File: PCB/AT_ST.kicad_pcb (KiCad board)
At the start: 2 copper layers, 127.3 x 96.8 mm, 84 parts, among them J1 4PIN, J2 OLED, J3 Conn_01x05_Female, J4 Conn_01x05_Female, SW1 SW1, SW10 SW10, SW11 SW11, SW12 SW12, SW13 SW13, SW14 SW14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

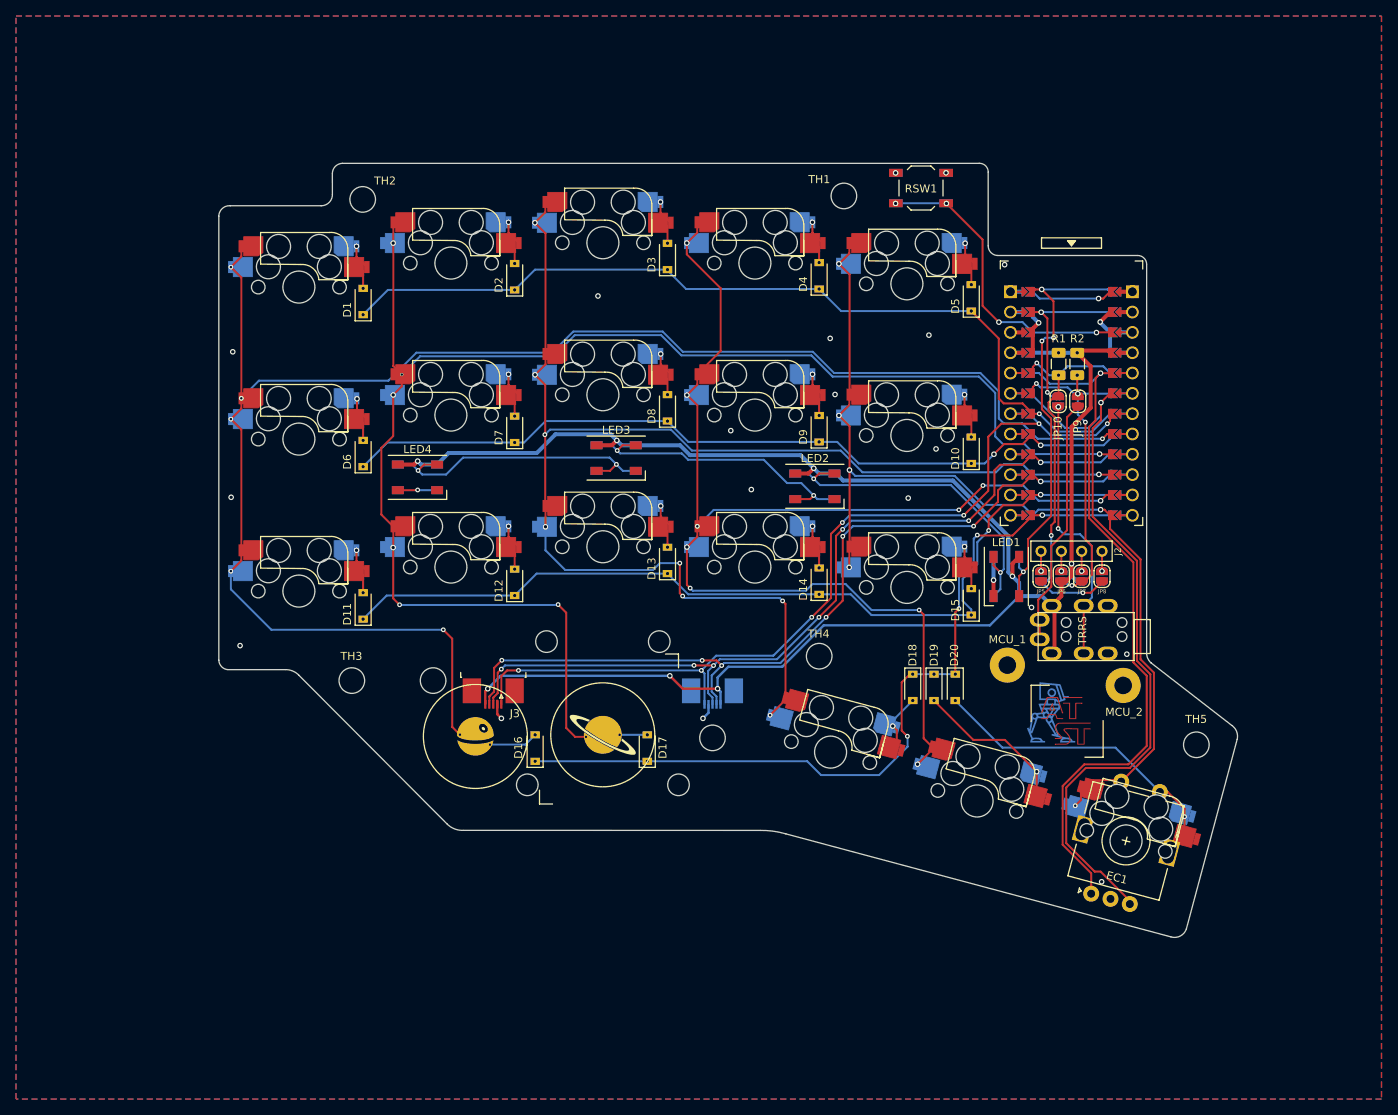
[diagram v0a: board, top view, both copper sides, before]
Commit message: 1. Correct a serious pin allocation problem, where a digital pin was assigned for joystick Y axis. 2. Updated MX switches footprints. 3. Included flip style 5 pins FPC/FFC socket. 4. Minor changes here and there.
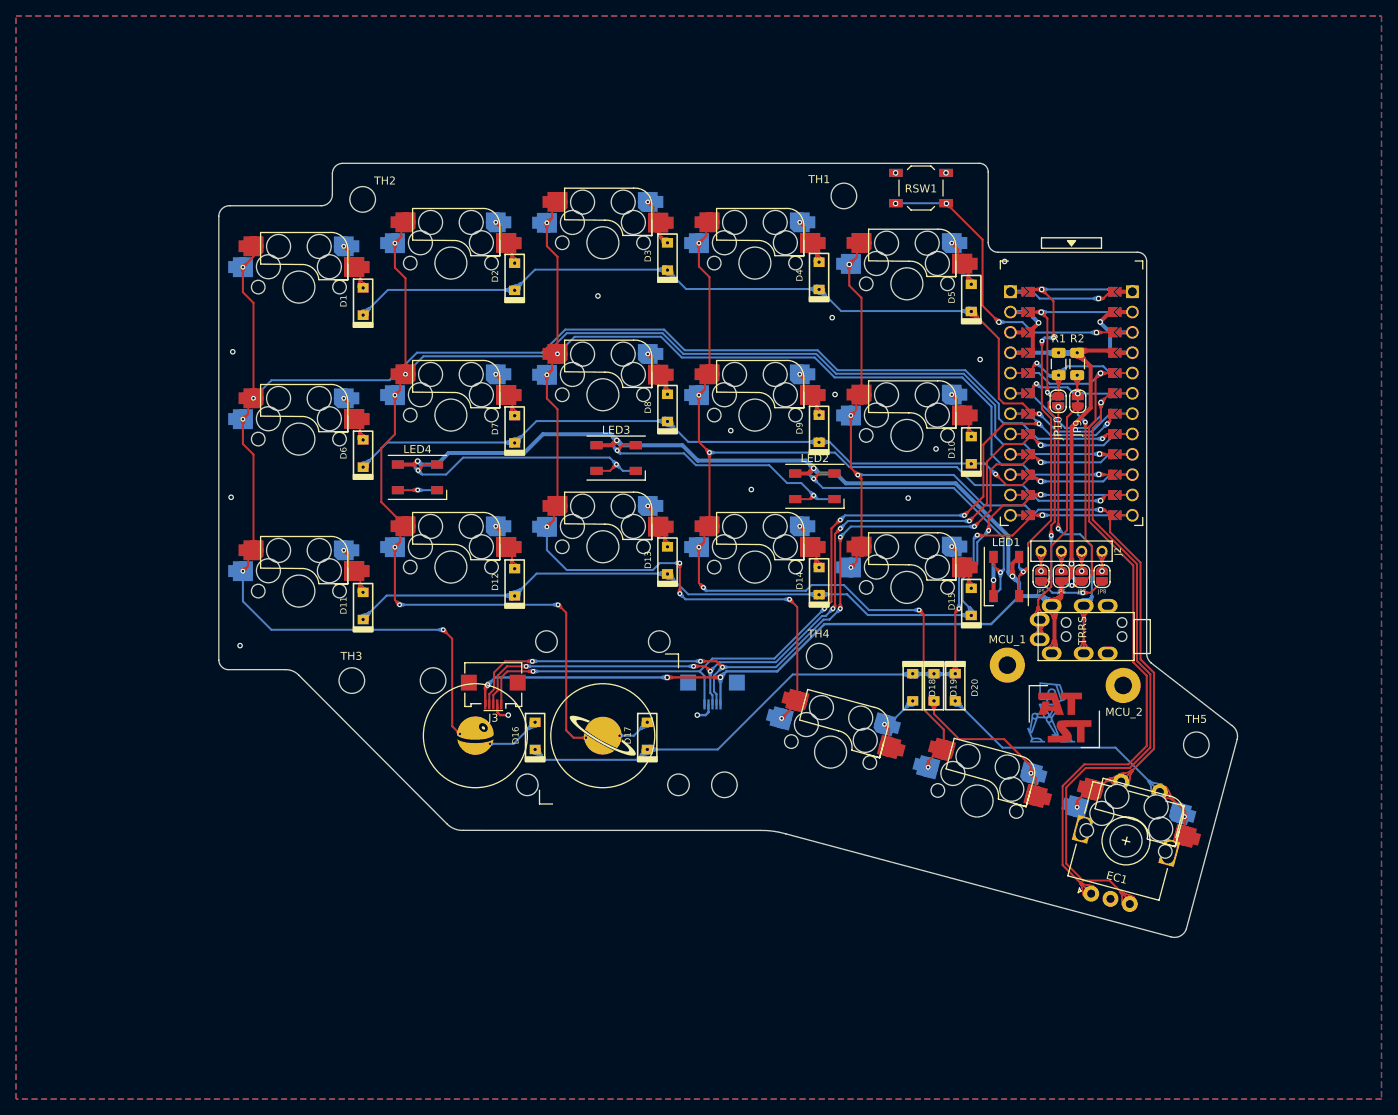
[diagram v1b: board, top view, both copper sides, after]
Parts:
- removed the REF** at (204.0, 128.3)
- added REF**: star_wars_at_st_text_f.cu, jw_custom_image:star_wars_at_st_text_f.cu, F.Cu at (203.8, 127.8)
- D1, D10, D11, D12, D13, D14, D15, D16, D17, D18, D19, D2, D20, D3, D4, D5, D6, D7, D8, D9: footprint jw_custom_footprint:Diode_SOD123_THT -> jw_custom_footprint:Diode_SOD123_THT_2
- J3, J4: footprint Connector_FFC-FPC:TE_0-1734839-5_1x05-1MP_P0.5mm_Horizontal -> jw_custom_footprint:Molex_200528-0050_1x05-1MP_P0.5mm_Horizontal
- moved JY_BT_2 6.05 mm to (161.1, 136.2)
- moved D16 1.52 mm to (137.5, 130.1)
- moved D17 1.52 mm to (151.5, 130.1)
- moved J3 0.44 mm to (132.2, 125.3)
- moved J4 0.44 mm to (159.6, 125.3)
- moved JY_CABLE_1 0.32 mm to (132.2, 117.9)
- moved JY_CABLE_2 0.32 mm to (159.6, 117.9)
- moved SW17 0.11 mm to (145.9, 130.1)
- moved SW16 0.09 mm to (130.0, 130.1)
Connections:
- net RESET renamed RST
- U1 pad 10: Axis_Y -> row1
- U1 pad 8: row1 -> BT
- U1 pad 9: BT -> Axis_Y
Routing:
- net col3: track 156.6 -> 148.8 mm, vias 10 -> 8
- net row3: track 100.4 -> 93.6 mm, vias 4 -> 3
- net col2: track 170.0 -> 176.1 mm
- net col0: track 208.0 -> 203.3 mm
- net col4: track 122.1 -> 118.2 mm
- net Axis_Y: track 103.8 -> 107.7 mm
- net BT: track 104.5 -> 107.7 mm
- net Net-(D19-Pad2): track 18.5 -> 20.5 mm
- net Net-(D13-Pad2): track 5.25 -> 3.34 mm
- net Net-(D14-Pad2): track 5.27 -> 3.44 mm
- net Net-(D9-Pad2): track 5.22 -> 3.39 mm
- net Net-(D8-Pad2): track 5.18 -> 3.42 mm
- net Net-(D11-Pad2): track 5.37 -> 3.62 mm
- net Net-(D15-Pad2): track 5.34 -> 3.61 mm
- net Net-(D10-Pad2): track 5.39 -> 3.66 mm
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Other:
- outline, holes or cut-outs redrawn
